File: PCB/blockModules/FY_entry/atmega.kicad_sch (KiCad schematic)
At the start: 12 parts, among them J1101 Conn_01x03, U201 HEADER_3x2, U202 ATmega328-A, Y201 Crystal_GND2

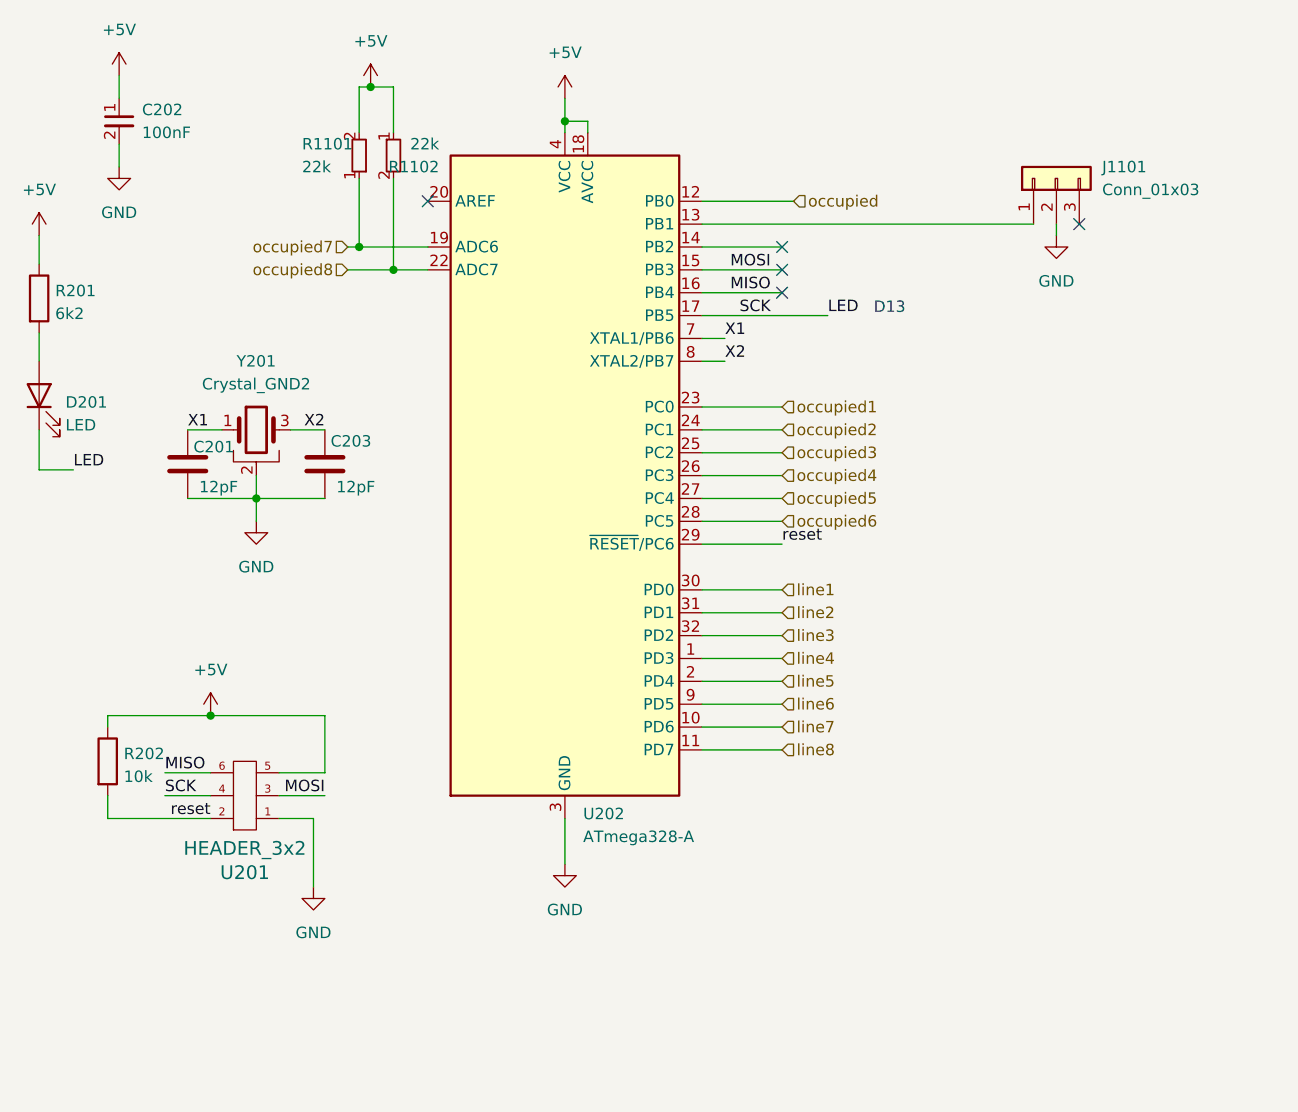
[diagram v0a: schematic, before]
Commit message: Added PDF files for all schematics
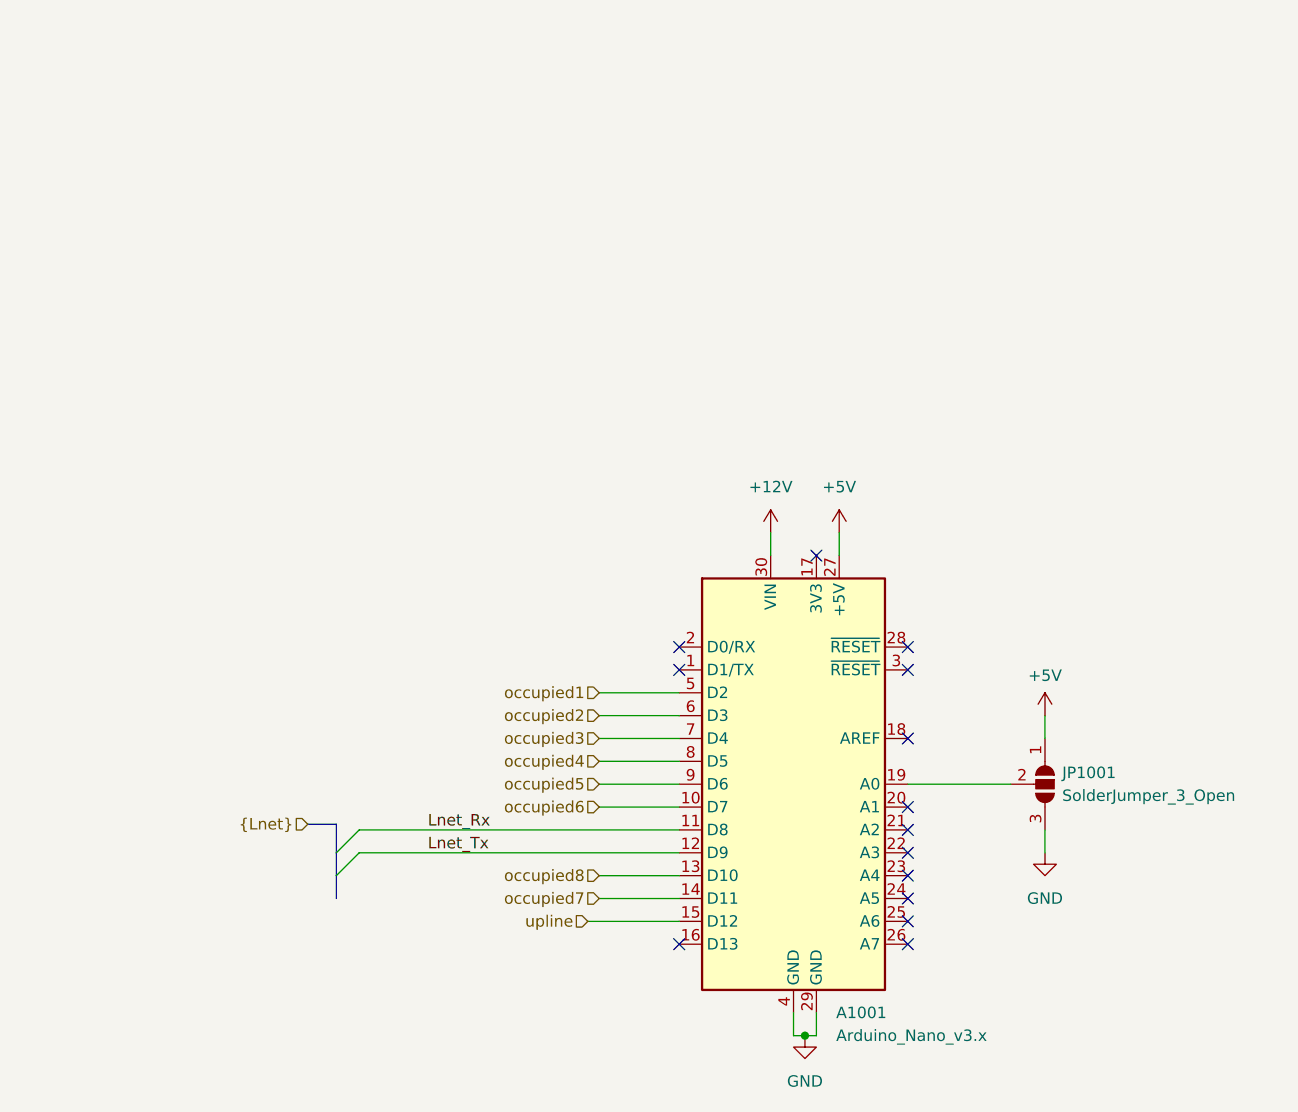
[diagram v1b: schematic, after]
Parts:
- removed C201, C203: 12pF, Capacitor_SMD:C_0603_1608Metric, symbol Device:C
- removed C202: 100nF, Capacitor_SMD:C_0402_1005Metric, symbol capacitor_miscellaneous:C_0402_100nF
- removed D201: LED, LED_SMD:LED_0805_2012Metric_Pad1.15x1.40mm_HandSolder, symbol Device:LED
- removed J1101: Conn_01x03, Connector_PinHeader_2.54mm:PinHeader_1x03_P2.54mm_Vertical, symbol Connector_Generic:Conn_01x03
- removed R1101, R1102: 22k, custom_kicad_lib_sk:R_0603_smalltext, symbol resistors_0603:R_22k_0603
- removed R201: 6k2, Resistor_SMD:R_0603_1608Metric_Pad0.98x0.95mm_HandSolder, symbol Device:R
- removed R202: 10k, Resistor_SMD:R_0402_1005Metric_Pad0.72x0.64mm_HandSolder, symbol Device:R
- removed U201: HEADER_3x2, Connector_PinSocket_1.27mm:PinSocket_2x03_P1.27mm_Vertical, symbol servoDriverSMD-rescue:HEADER_3x2-w_connectors
- removed U202: ATmega328-A, Package_QFP:TQFP-32_7x7mm_P0.8mm, symbol MCU_Microchip_ATmega:ATmega328-A
- removed Y201: Crystal_GND2, custom_kicad_lib_sk:crystal_arduino, symbol custom_kicad_lib_sk:crystal_arduino
- added A1001: Arduino_Nano_v3.x, Module:Arduino_Nano, symbol MCU_Module:Arduino_Nano_v3.x
- added JP1001: SolderJumper_3_Open, Jumper:SolderJumper-3_P1.3mm_Open_RoundedPad1.0x1.5mm, symbol Jumper:SolderJumper_3_Open
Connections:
- net +5V: now also A1001.27 (+5V), JP1001.1 (A)
- net GND: now also A1001.29 (GND), A1001.4 (GND), JP1001.3 (B)
- net occupied1: now also A1001.5 (D2)
- net occupied2: now also A1001.6 (D3)
- net occupied3: now also A1001.7 (D4)
- net occupied4: now also A1001.8 (D5)
- net occupied5: now also A1001.9 (D6)
- net occupied6: now also A1001.10 (D7)
- net occupied7: now also A1001.14 (D11)
- net occupied8: now also A1001.13 (D10)
- new net: A1001.19 (A0), JP1001.2 (C)
- new net +12V: A1001.30 (VIN)
- new net Lnet_Rx: A1001.11 (D8)
- new net Lnet_Tx: A1001.12 (D9)
- new net upline: A1001.15 (D12)
- no-connect marks 5 -> 14
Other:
- note removed: "D13"
